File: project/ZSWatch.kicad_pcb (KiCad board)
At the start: 4 copper layers, 41 x 38 mm, 94 parts, among them IC101 nPM1300-QEXX, IC201 APDS-9306-065, IC202 BMI270, IC203 BMP581, IC204 LIS2MDLTR, IC205 BME688, IC301 ESDALC6V1W5, IC302 FAN5622SX, IC303 MX25U51245GZ4I00, IC304 TS3USB221A, IC305 NTS0104GU12, IC306 DRV2603RUNT, IC307 RV-8263-C8, M301 NORA-B106, Q201 DMG1013UW-7, Q301 BC817W, Q302 PMZ550UNEYL, Q303 PMZ550UNEYL, X101 BATTERY, X301 DOCK, X302 GC9A01A_CST816S, X303 M+, X304 M-

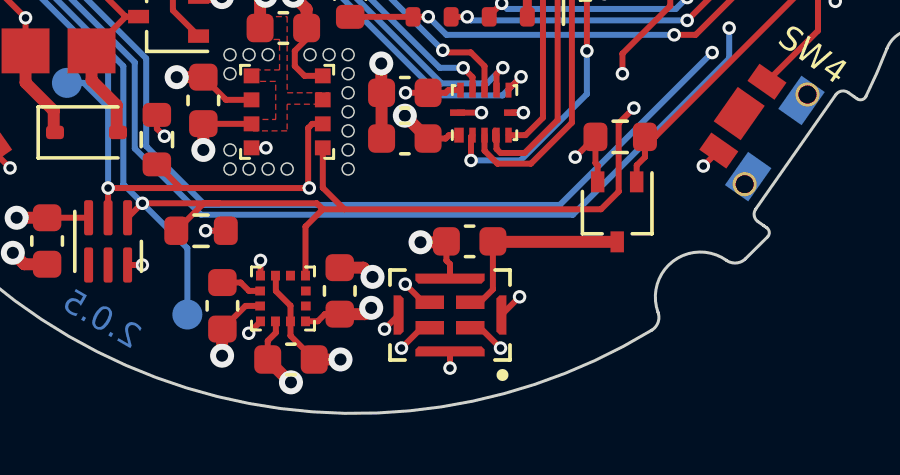
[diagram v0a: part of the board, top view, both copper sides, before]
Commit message: Update footprints
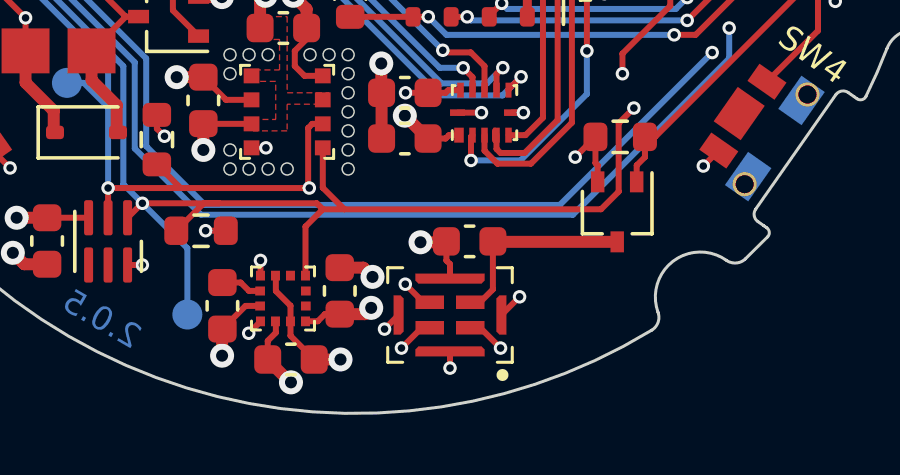
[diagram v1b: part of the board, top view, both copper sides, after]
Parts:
- moved M301 0.10 mm to (174.6, 112.7)

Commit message: Fix wrong transistors for I2C level shifter
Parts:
- moved Q303 0.43 mm to (166.2, 104.6), turned to 0 degrees
- moved Q302 0.20 mm to (164.6, 103.7), turned to 0 degrees
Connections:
- Q302 pad 2: Net-(IC307-SCL) -> /MCU/SENSOR-SCL
- Q302 pad 3: /MCU/SENSOR-SCL -> Net-(IC307-SCL)
- Q303 pad 2: Net-(IC307-SDA) -> /MCU/SENSOR-SDA
- Q303 pad 3: /MCU/SENSOR-SDA -> Net-(IC307-SDA)

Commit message: Change layer for PCB tables to User1
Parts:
- moved R102 0.16 mm to (166.9, 102.9)
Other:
- board text added: "0,9820 mm"
- board text added: "40,9576 mm x 37,9989 mm"
- board text added: "Dielektrikum"
- board text added: "Tangens des Verlustwinkels"
- board text removed: "0,9800 mm"
- board text removed: "40,9601 mm x 37,9900 mm"
- board text removed: "Dielektrikum 1"
- board text removed: "Dielektrikum 2"
- board text removed: "Dielektrikum 3"
- board text removed: "Verlustfaktor"

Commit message: Rename signals and update symbols and footprints
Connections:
- net /MCU/VBAT renamed /MCU/V_{BAT}
- net /MCU/VBUS-MCU renamed /MCU/V_{BUS}-MCU
- net /MCU/VDD-Display renamed /MCU/V_{DD}-Display
- net /MCU/VSYS renamed /MCU/V_{SYS}
- net VBUS renamed /MCU/V_{BUS}

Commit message: - Switch to a local KiCad library
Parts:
- IC101: footprint Package_DFN_QFN:QFN-32-1EP_5x5mm_P0.5mm_EP3.6x3.6mm_ThermalVias -> Package_DFN_QFN:QFN-32-1EP_5x5mm_P0.5mm_EP3.6x3.6mm
- IC202: footprint Package_LGA_Kampi:Bosch_LGA-14_3x2.5mm_P0.5mm_LayoutBorder3x4y -> Package_LGA:Bosch_LGA-14_3x2.5mm_P0.5mm_LayoutBorder3x4y
- IC203: footprint Package_LGA_Kampi:Bosch_LGA-10_2x2mm_P0.5mm_ClockwisePinNumbering -> Package_LGA:Bosch_LGA-10_2x2mm_P0.5mm_ClockwisePinNumbering
- IC204: footprint Package_LGA_Kampi:LGA-12_2x2mm_P0.5mm -> Package_LGA:LGA-12_2x2mm_P0.5mm
- IC205: footprint Package_LGA_Kampi:Bosch_LGA-8_3x3mm_P0.8mm_ClockwisePinNumbering -> Package_LGA:Bosch_LGA-8_3x3mm_P0.8mm_ClockwisePinNumbering
- L101, L102: footprint Inductor_SMD_Kampi:L_0806_2016 -> Inductor_SMD:L_0806_2016

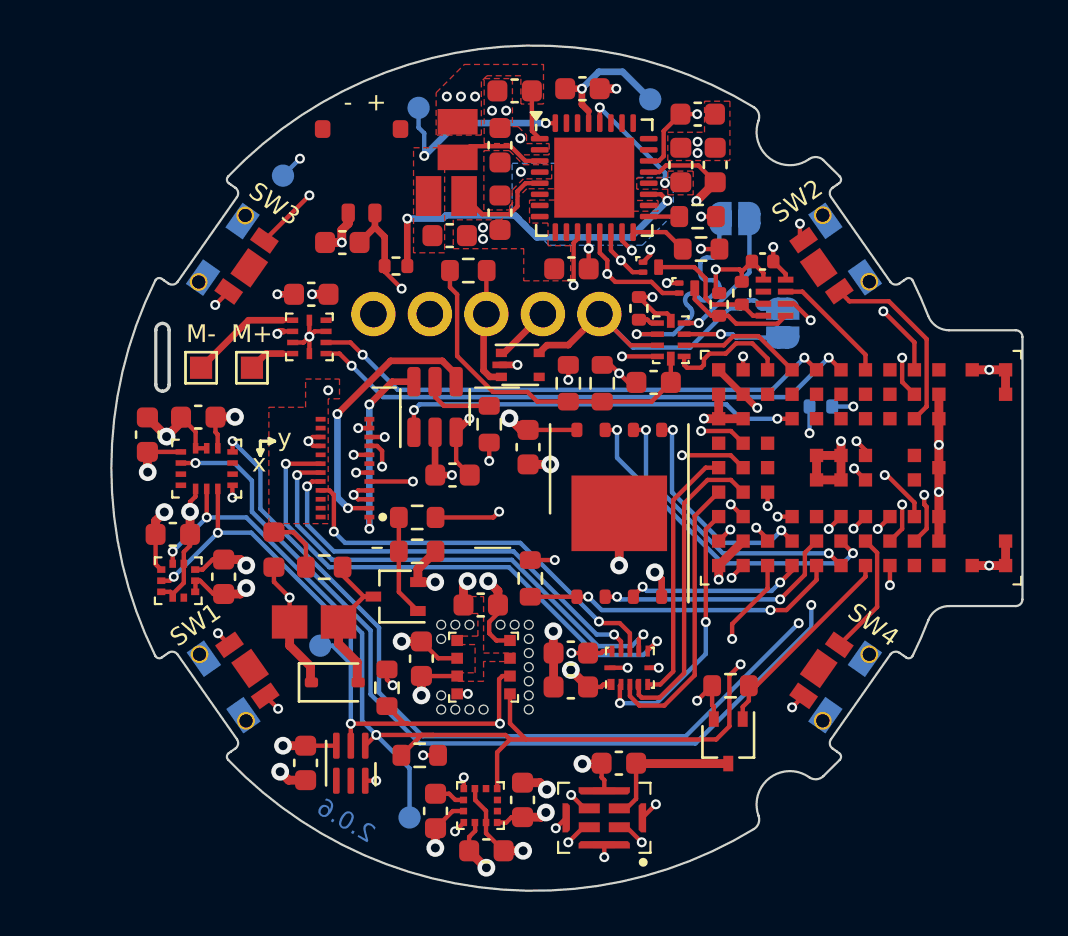
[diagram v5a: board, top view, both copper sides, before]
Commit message: Add new vibration motor
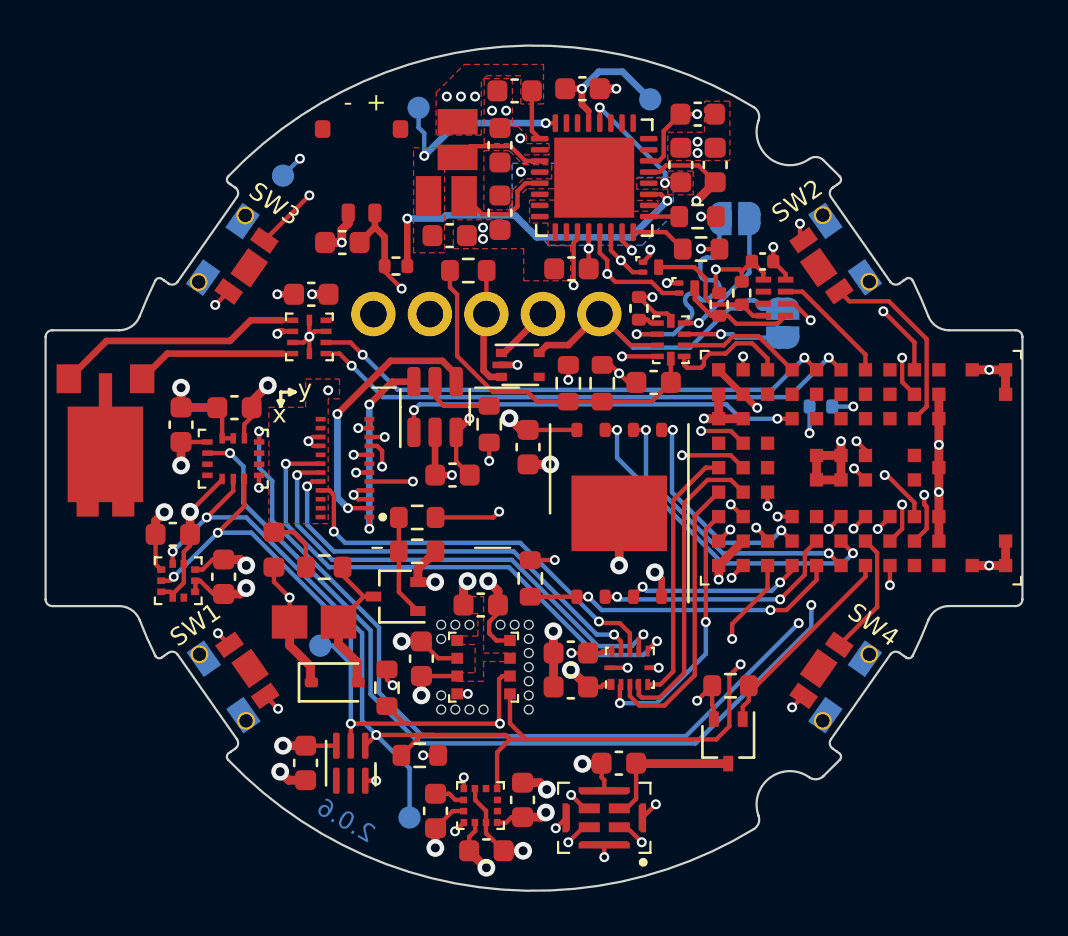
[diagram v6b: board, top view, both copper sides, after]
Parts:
- removed X303: M+, TestPoint:TestPoint_Pad_1.0x1.0mm
- removed X304: M-, TestPoint:TestPoint_Pad_1.0x1.0mm
- added M302: Vibration Motor, Vybronics:VZ30C1T8219732L, F.Cu at (140.1, 111.8)
- moved C202 1.68 mm to (145.9, 110.0)
- moved C203 1.58 mm to (143.5, 110.8)
- moved IC202 1.27 mm to (145.8, 112.3)
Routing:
- net Net-(IC306-OUT-): track 5.00 -> 11.2 mm
- net Net-(IC306-OUT+): track 2.10 -> 7.24 mm
- net +1V8: track 47.2 -> 48.6 mm
- net /MCU/SENSOR-SDA: track 83.8 -> 84.7 mm
- net /MCU/SENSOR-SCL: track 88.8 -> 89.7 mm
- net /MCU/BMI270-INT2: track 48.1 -> 47.2 mm
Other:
- board size 41 x 38 mm -> 43.9 x 38 mm

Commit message: Fix wrong footprint path in symbols, add new vibration motor to PCB
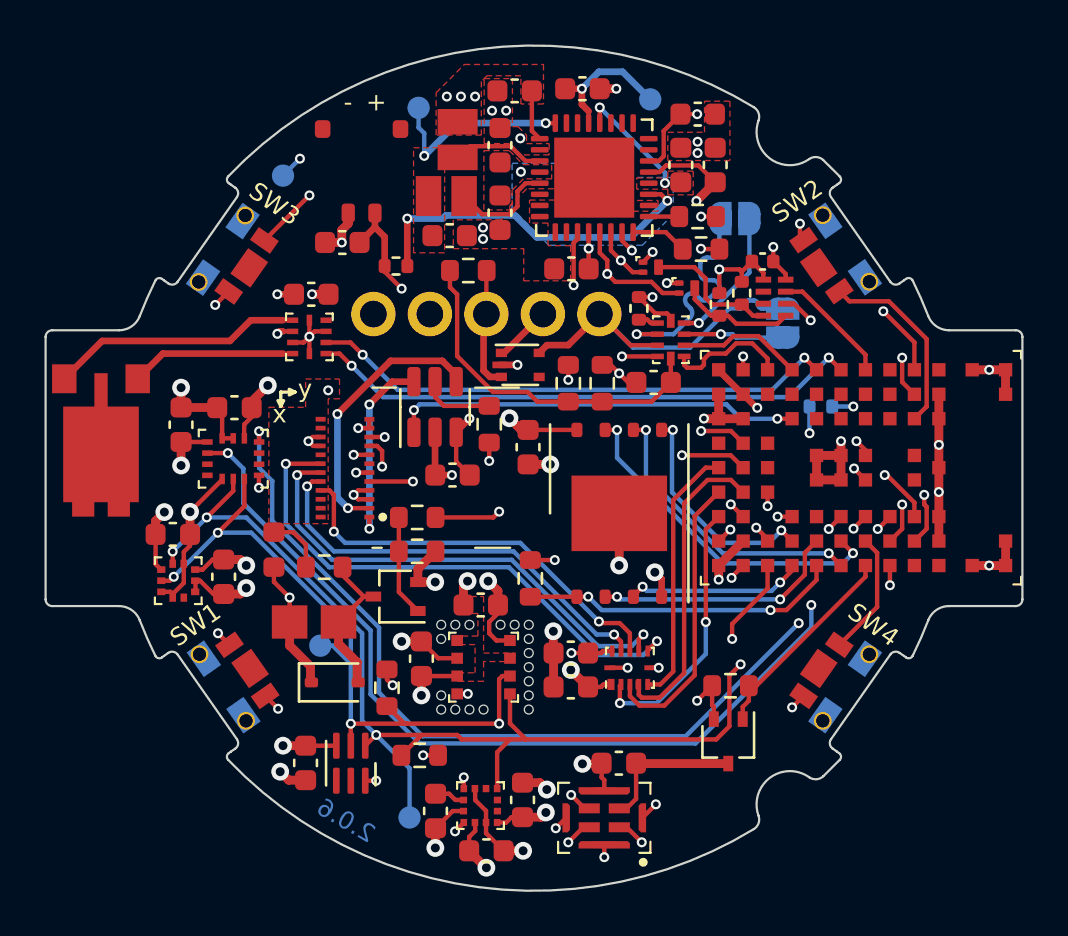
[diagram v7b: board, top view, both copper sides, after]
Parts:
- moved M302 0.20 mm to (139.9, 111.8)
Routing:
- net /MCU/SENSOR-SCL: track 89.7 -> 89.2 mm

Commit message: Display is now supplied with 3V0, add current consumption overview, vibration motor is now supplied with 3V0, add 0R series resistor for buzzer
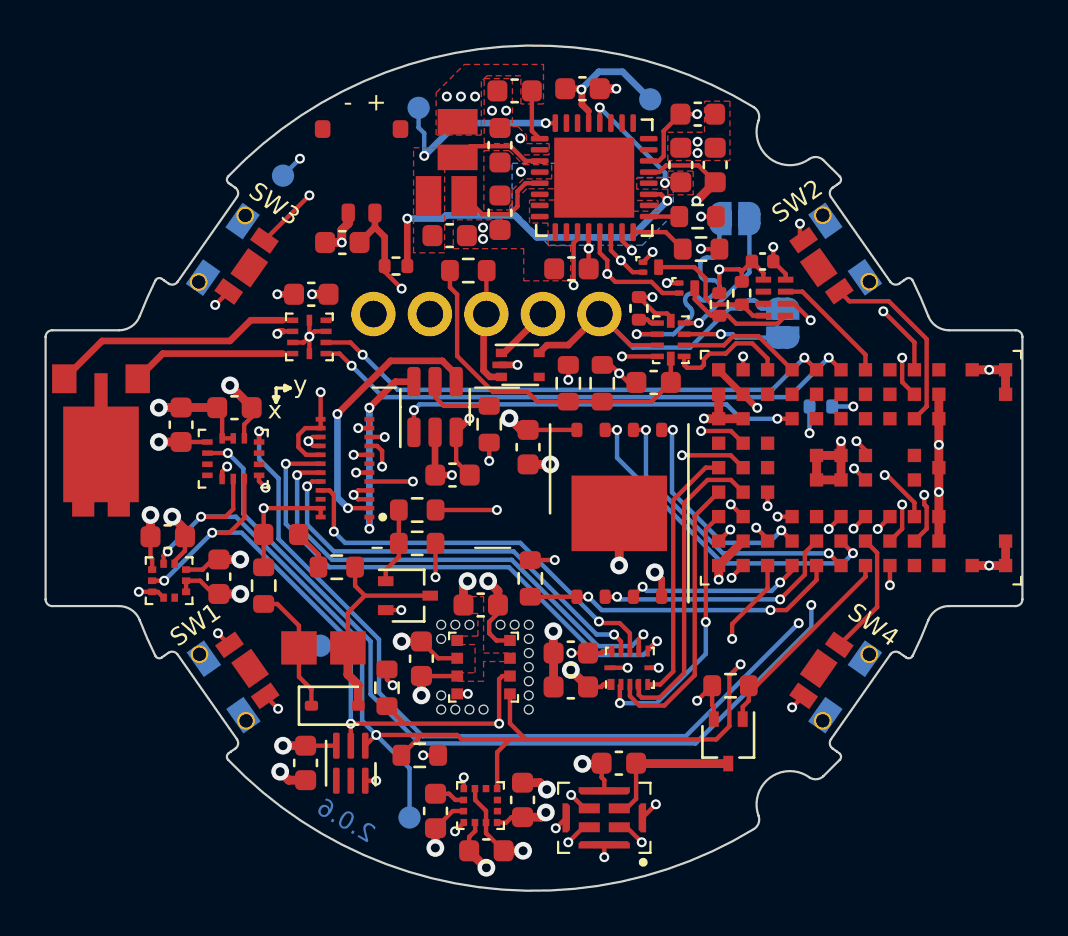
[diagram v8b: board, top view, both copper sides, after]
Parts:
- added R401: 0R, Resistor_SMD:R_0603_1608Metric, F.Cu at (147.2, 118.0)
- moved BZ301 1.24 mm to (149.9, 120.8)
- moved D301 1.05 mm to (150.4, 123.4)
- moved D302 0.76 mm to (148.0, 115.7), turned to 180 degrees
- moved R314 0.56 mm to (150.5, 117.2)
- moved Q301 0.56 mm to (153.7, 118.5), turned to 0 degrees
- moved IC203 0.41 mm to (143.0, 117.8)
- moved R307 0.36 mm to (154.1, 116.1)
- moved R311 0.34 mm to (154.1, 114.6)
- moved C207 0.25 mm to (142.9, 115.8)
- moved C206 0.22 mm to (145.2, 117.6)
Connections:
- BZ301 pad 1: +3V0 -> Net-(BZ301-+)
- C104 pad 1: /MCU/V_{SYS} -> /Power Management/V_{SYS}
- C106 pad 1: /MCU/V_{SYS} -> /Power Management/V_{SYS}
- C108 pad 1: /MCU/V_{DD}-Display -> Net-(IC101-LSOUT1/VOUTLDO1)
- C109 pad 1: /MCU/V_{SYS} -> /Power Management/V_{SYS}
- C301 pad 2: /MCU/V_{DD}-Display -> +3V0
- C305 pad 1: /MCU/V_{DD}-Display -> +3V0
- C306 pad 1: /MCU/V_{SYS} -> +3V0
- D301 pad 1: +3V0 -> Net-(BZ301-+)
- IC101 pad 20: /MCU/V_{SYS} -> /Power Management/V_{SYS}
- IC101 pad 28: /MCU/V_{SYS} -> /Power Management/V_{SYS}
- IC101 pad 29: /MCU/V_{DD}-Display -> Net-(IC101-LSOUT1/VOUTLDO1)
- IC101 pad 4: /MCU/V_{SYS} -> /Power Management/V_{SYS}
- IC302 pad 3: /MCU/V_{DD}-Display -> +3V0
- IC305 pad 11: /MCU/V_{DD}-Display -> +3V0
- IC306 pad 7: /MCU/V_{SYS} -> +3V0
- TP103 pad 1: /MCU/V_{DD}-Display -> Net-(IC101-LSOUT1/VOUTLDO1)
- X302 pad 13: /MCU/V_{DD}-Display -> +3V0
- X302 pad 14: /MCU/V_{DD}-Display -> +3V0
- X302 pad 17: /MCU/V_{DD}-Display -> +3V0
- X302 pad 23: /MCU/V_{DD}-Display -> +3V0
- X302 pad 24: /MCU/V_{DD}-Display -> +3V0
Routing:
- net /MCU/V_{DD}-Display: track 52.1 -> 0.00 mm, vias 4 -> 0
- net /MCU/V_{SYS}: track 28.3 -> 0.00 mm, vias 5 -> 0
- net +3V0: track 39.8 -> 68.1 mm, vias 3 -> 8
- net Net-(IC101-LSOUT1/VOUTLDO1): track 0.00 -> 6.34 mm, vias 0 -> 1
- net Net-(BZ301-+): track 0.00 -> 5.82 mm
- net /Power Management/V_{SYS}: track 0.00 -> 5.32 mm, vias 0 -> 3
- net Net-(BZ301--): track 6.78 -> 9.85 mm
- net +1V8: track 48.5 -> 46.3 mm, vias 25 -> 27
- net Net-(Q301-B): track 4.56 -> 3.44 mm
- net /MCU/SENSOR-SCL: track 89.2 -> 90.1 mm
- net Net-(D302-K): track 2.68 -> 1.84 mm
- net /MCU/SENSOR-SDA: track 84.7 -> 85.5 mm
- net GND: track 87.9 -> 87.7 mm, vias 55 -> 56
- added copper zone on B.Cu, net /Power Management/V_{SYS}
- added copper zone on F.Cu, net /Power Management/V_{SYS}
- removed copper zone on F.Cu, net /MCU/V_{DD}-Display
- removed copper zone on B.Cu, net /MCU/V_{SYS}
- removed copper zone on F.Cu, net /MCU/V_{SYS}
